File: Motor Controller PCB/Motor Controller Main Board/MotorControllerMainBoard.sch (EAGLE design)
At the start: 83 parts, among them T1 TEENSY_3.1_ALL_PINS

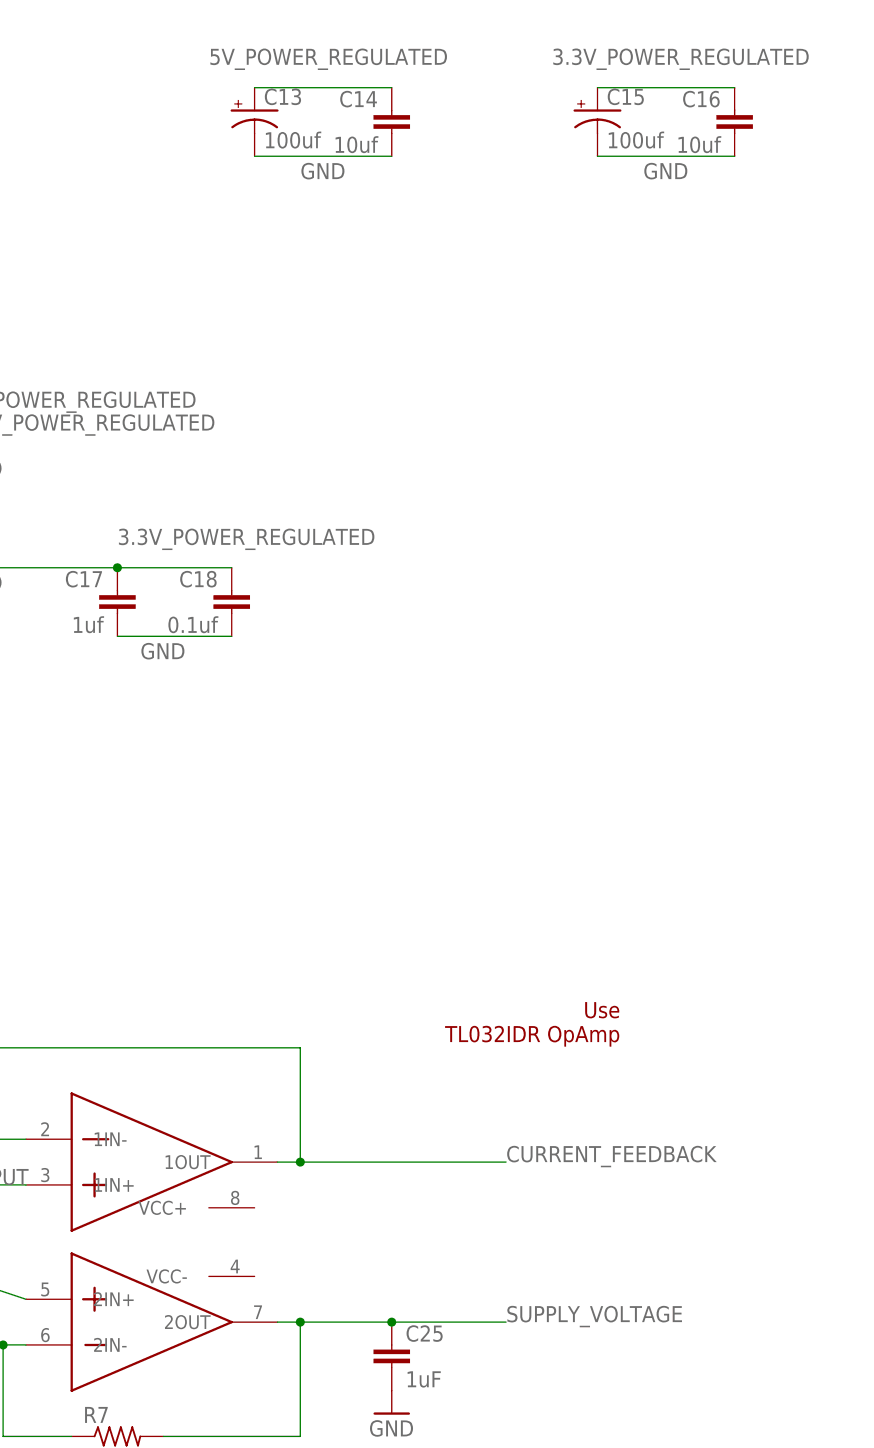
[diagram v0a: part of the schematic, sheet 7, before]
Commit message: Paralleled power capacitors for the teensy
-For both the 5V and 3.3V
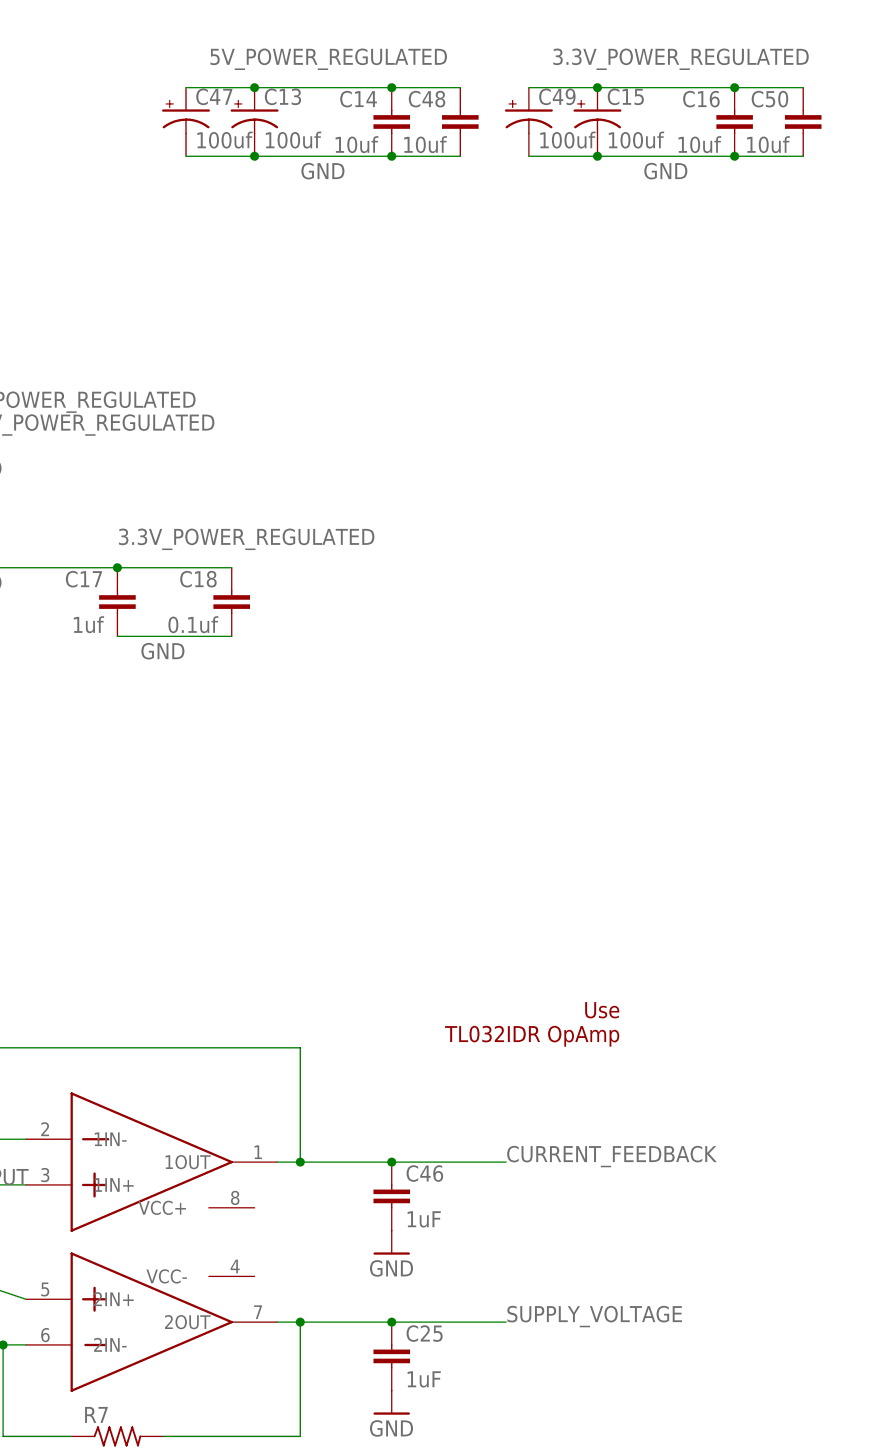
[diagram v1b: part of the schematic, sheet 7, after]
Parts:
- added C46: 1uF, rcl:C-EUC0805
- added C47, C49: 100uf, SparkFun-Capacitors:CAP_POLC
- added C48, C50: 10uf, SparkFun-Capacitors:CAP0805
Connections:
- net 3.3V_POWER_REGULATED: now also C49.+, C50.1
- net 5V_POWER_REGULATED: now also C47.+, C48.1
- net CURRENT_FEEDBACK: now also C46.1
- net GND: now also C46.2, C47.-, C48.2, C49.-, C50.2
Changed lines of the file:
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@@
 <part name="R11" library="MotorControllerEagleLibrary" deviceset="FKN1WSJR-52-4R7" device=""/>
 <part name="R12" library="MotorControllerEagleLibrary" deviceset="FKN1WSJR-52-4R7" device=""/>
+<part name="C46" library="rcl" deviceset="C-EU" device="C0805" value="1uF"/>
+<part name="GND27" library="E-P-008-R1.2" deviceset="GND" device=""/>
+<part name="C47" library="SparkFun-Capacitors" deviceset="CAP_POL" device="C" value="100uf"/>
+<part name="C48" library="SparkFun-Capacitors" deviceset="CAP" device="0805" value="10uf"/>
+<part name="C49" library="SparkFun-Capacitors" deviceset="CAP_POL" device="C" value="100uf"/>
+<part name="C50" library="SparkFun-Capacitors" deviceset="CAP" device="0805" value="10uf"/>
 </parts>
 <sheets>
@@
 <instance part="C23" gate="G$1" x="134.62" y="60.96"/>
 <instance part="GND9" gate="1" x="134.62" y="53.34"/>
+<instance part="C46" gate="G$1" x="213.36" y="76.2"/>
+<instance part="GND27" gate="1" x="213.36" y="68.58"/>
+<instance part="C47" gate="G$1" x="190.5" y="195.58"/>
+<instance part="C48" gate="G$1" x="220.98" y="193.04" rot="MR0"/>
+<instance part="C49" gate="G$1" x="228.6" y="195.58"/>
+<instance part="C50" gate="G$1" x="259.08" y="193.04" rot="MR0"/>
 </instances>
 <busses>
@@
 <label x="203.2" y="187.96" size="1.778" layer="95"/>
 <pinref part="C14" gate="G$1" pin="2"/>
+<pinref part="C47" gate="G$1" pin="-"/>
+<wire x1="190.5" y1="190.5" x2="198.12" y2="190.5" width="0.1524" layer="91"/>
+<junction x="198.12" y="190.5"/>
+<pinref part="C48" gate="G$1" pin="2"/>
+<wire x1="213.36" y1="190.5" x2="220.98" y2="190.5" width="0.1524" layer="91"/>
+<junction x="213.36" y="190.5"/>
 </segment>
 <segment>
@@
 <label x="241.3" y="187.96" size="1.778" layer="95"/>
 <pinref part="C16" gate="G$1" pin="2"/>
+<pinref part="C49" gate="G$1" pin="-"/>
+<wire x1="228.6" y1="190.5" x2="236.22" y2="190.5" width="0.1524" layer="91"/>
+<junction x="236.22" y="190.5"/>
+<pinref part="C50" gate="G$1" pin="2"/>
+<wire x1="251.46" y1="190.5" x2="259.08" y2="190.5" width="0.1524" layer="91"/>
+<junction x="251.46" y="190.5"/>
 </segment>
 <segment>
@@
 <pinref part="GND9" gate="1" pin="GND"/>
 </segment>
+<segment>
+<pinref part="C46" gate="G$1" pin="2"/>
+<pinref part="GND27" gate="1" pin="GND"/>
+</segment>
 </net>
 <net name="5V_POWER_REGULATED" class="0">
@@
 <wire x1="198.12" y1="198.12" x2="213.36" y2="198.12" width="0.1524" layer="91"/>
 <label x="193.04" y="200.66" size="1.778" layer="95"/>
+<pinref part="C47" gate="G$1" pin="+"/>
+<wire x1="190.5" y1="198.12" x2="198.12" y2="198.12" width="0.1524" layer="91"/>
+<junction x="198.12" y="198.12"/>
+<pinref part="C48" gate="G$1" pin="1"/>
+<wire x1="213.36" y1="198.12" x2="220.98" y2="198.12" width="0.1524" layer="91"/>
+<junction x="213.36" y="198.12"/>
 </segment>
 <segment>
@@
 <wire x1="236.22" y1="198.12" x2="251.46" y2="198.12" width="0.1524" layer="91"/>
 <label x="231.14" y="200.66" size="1.778" layer="95"/>
+<pinref part="C49" gate="G$1" pin="+"/>
+<wire x1="228.6" y1="198.12" x2="236.22" y2="198.12" width="0.1524" layer="91"/>
+<junction x="236.22" y="198.12"/>
+<pinref part="C50" gate="G$1" pin="1"/>
+<wire x1="251.46" y1="198.12" x2="259.08" y2="198.12" width="0.1524" layer="91"/>
+<junction x="251.46" y="198.12"/>
 </segment>
 <segment>
@@
 <wire x1="203.2" y1="78.74" x2="200.66" y2="78.74" width="0.1524" layer="91"/>
 <junction x="203.2" y="78.74"/>
-<wire x1="203.2" y1="78.74" x2="226.06" y2="78.74" width="0.1524" layer="91"/>
+<wire x1="203.2" y1="78.74" x2="213.36" y2="78.74" width="0.1524" layer="91"/>
 <label x="226.06" y="78.74" size="1.778" layer="95"/>
-</segment>
-</net>
+<pinref part="C46" gate="G$1" pin="1"/>
+<wire x1="213.36" y1="78.74" x2="226.06" y2="78.74" width="0.1524" layer="91"/>
+<junction x="213.36" y="78.74"/>
+</segment>
+</net>

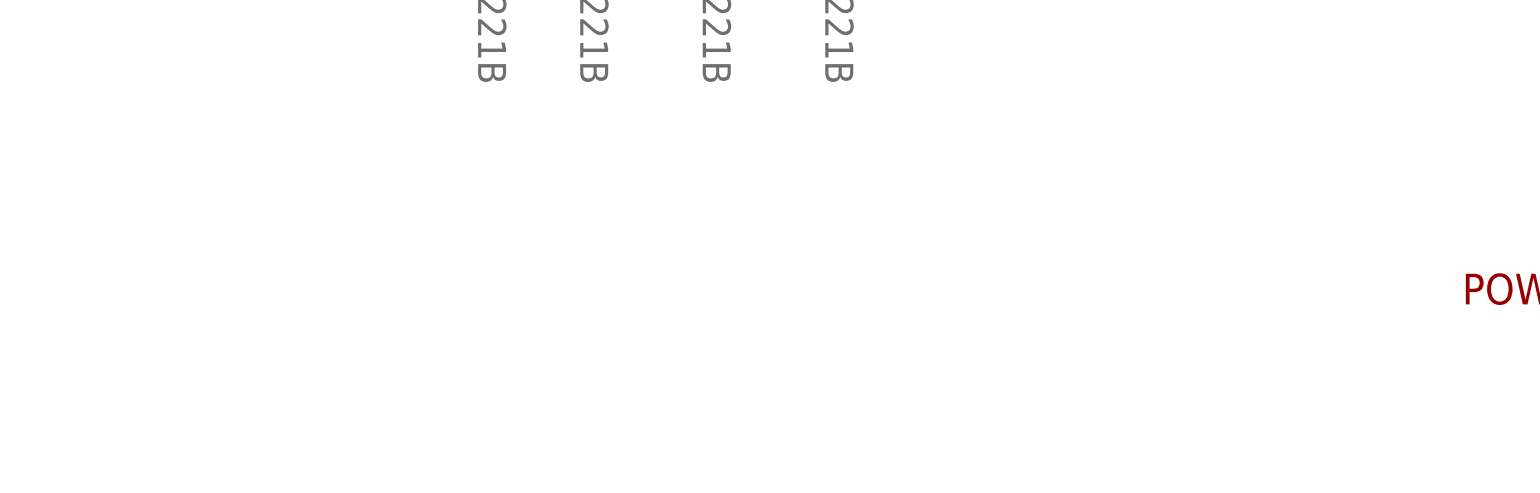
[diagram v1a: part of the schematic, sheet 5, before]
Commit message: Added Negative 12V regulator for op-amps
-Added a -12V regulator for the op-amps. Low power, simple charge pump
that inverts the 12V regulator that already exists on the board.
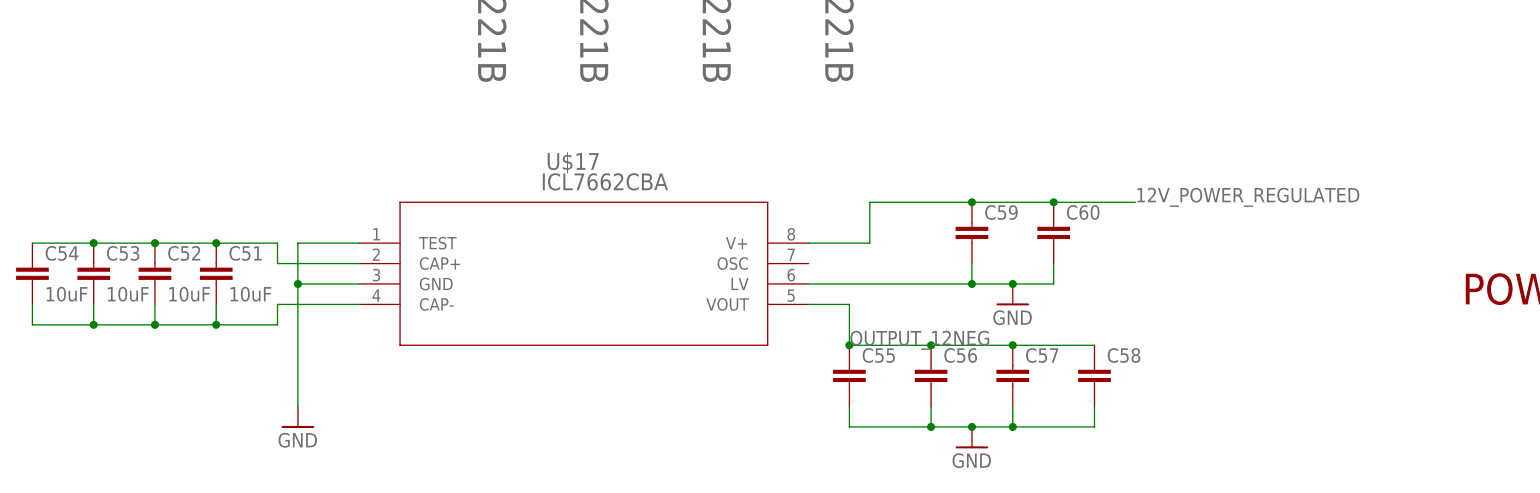
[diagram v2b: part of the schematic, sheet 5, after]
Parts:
- added C51, C52, C53, C54: 10uF, resistor:C-EUC0805
- added C55, C56, C57, C58, C59, C60: (no value), resistor:C-EUC0805
- added U$17: ICL7662CBA, linear:ICL7662CBA
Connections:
- new net N$14: C51.1, C52.1, C53.1, C54.1, U$17.CAP+
- new net N$15: C51.2, C52.2, C53.2, C54.2, U$17.CAP-
- new net OUTPUT_12NEG: AD8512ARZ.VCC-, C55.1, C56.1, C57.1, C58.1, U$17.VOUT
- net 12V_POWER_REGULATED: now also AD8512ARZ.VCC+, C59.1, C60.1, U$17.V+
- net GND: now also C55.2, C56.2, C57.2, C58.2, C59.2, C60.2, U$17.GND, U$17.LV, U$17.TEST
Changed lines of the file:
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@@
 <part name="C49" library="SparkFun-Capacitors" deviceset="CAP_POL" device="C" value="100uf"/>
 <part name="C50" library="SparkFun-Capacitors" deviceset="CAP" device="0805" value="10uf"/>
+<part name="U$17" library="linear" deviceset="ICL7662CBA" device=""/>
+<part name="GND28" library="E-P-008-R1.2" deviceset="GND" device=""/>
+<part name="C51" library="resistor" library_urn="urn:adsk.eagle:library:348" deviceset="C-EU" device="C0805" package3d_urn="urn:adsk.eagle:package:26137/1" value="10uF"/>
+<part name="C52" library="resistor" library_urn="urn:adsk.eagle:library:348" deviceset="C-EU" device="C0805" package3d_urn="urn:adsk.eagle:package:26137/1" value="10uF"/>
+<part name="C53" library="resistor" library_urn="urn:adsk.eagle:library:348" deviceset="C-EU" device="C0805" package3d_urn="urn:adsk.eagle:package:26137/1" value="10uF"/>
+<part name="C54" library="resistor" library_urn="urn:adsk.eagle:library:348" deviceset="C-EU" device="C0805" package3d_urn="urn:adsk.eagle:package:26137/1" value="10uF"/>
+<part name="C55" library="resistor" library_urn="urn:adsk.eagle:library:348" deviceset="C-EU" device="C0805" package3d_urn="urn:adsk.eagle:package:26137/1"/>
+<part name="C56" library="resistor" library_urn="urn:adsk.eagle:library:348" deviceset="C-EU" device="C0805" package3d_urn="urn:adsk.eagle:package:26137/1"/>
+<part name="C57" library="resistor" library_urn="urn:adsk.eagle:library:348" deviceset="C-EU" device="C0805" package3d_urn="urn:adsk.eagle:package:26137/1"/>
+<part name="C58" library="resistor" library_urn="urn:adsk.eagle:library:348" deviceset="C-EU" device="C0805" package3d_urn="urn:adsk.eagle:package:26137/1"/>
+<part name="C59" library="resistor" library_urn="urn:adsk.eagle:library:348" deviceset="C-EU" device="C0805" package3d_urn="urn:adsk.eagle:package:26137/1"/>
+<part name="C60" library="resistor" library_urn="urn:adsk.eagle:library:348" deviceset="C-EU" device="C0805" package3d_urn="urn:adsk.eagle:package:26137/1"/>
+<part name="GND29" library="E-P-008-R1.2" deviceset="GND" device=""/>
+<part name="GND30" library="E-P-008-R1.2" deviceset="GND" device=""/>
 </parts>
 <sheets>
@@
 <instance part="GND22" gate="1" x="66.04" y="99.06"/>
 <instance part="GND23" gate="1" x="66.04" y="172.72"/>
+<instance part="U$17" gate="G$1" x="60.96" y="35.56"/>
+<instance part="GND28" gate="1" x="55.88" y="12.7"/>
+<instance part="C51" gate="G$1" x="45.72" y="33.02"/>
+<instance part="C52" gate="G$1" x="38.1" y="33.02"/>
+<instance part="C53" gate="G$1" x="30.48" y="33.02"/>
+<instance part="C54" gate="G$1" x="22.86" y="33.02"/>
+<instance part="C55" gate="G$1" x="124.46" y="20.32"/>
+<instance part="C56" gate="G$1" x="134.62" y="20.32"/>
+<instance part="C57" gate="G$1" x="144.78" y="20.32"/>
+<instance part="C58" gate="G$1" x="154.94" y="20.32"/>
+<instance part="C59" gate="G$1" x="139.7" y="38.1"/>
+<instance part="C60" gate="G$1" x="149.86" y="38.1"/>
+<instance part="GND29" gate="1" x="144.78" y="27.94"/>
+<instance part="GND30" gate="1" x="139.7" y="10.16"/>
 </instances>
 <busses>
@@
 <pinref part="U$13" gate="A" pin="GND"/>
 <pinref part="GND22" gate="1" pin="GND"/>
+</segment>
+<segment>
+<pinref part="U$17" gate="G$1" pin="TEST"/>
+<wire x1="63.5" y1="35.56" x2="55.88" y2="35.56" width="0.1524" layer="91"/>
+<wire x1="55.88" y1="35.56" x2="55.88" y2="30.48" width="0.1524" layer="91"/>
+<pinref part="U$17" gate="G$1" pin="GND"/>
+<wire x1="55.88" y1="30.48" x2="55.88" y2="15.24" width="0.1524" layer="91"/>
+<wire x1="63.5" y1="30.48" x2="55.88" y2="30.48" width="0.1524" layer="91"/>
+<junction x="55.88" y="30.48"/>
+<pinref part="GND28" gate="1" pin="GND"/>
+</segment>
+<segment>
+<pinref part="U$17" gate="G$1" pin="LV"/>
+<pinref part="C59" gate="G$1" pin="2"/>
+<wire x1="119.38" y1="30.48" x2="139.7" y2="30.48" width="0.1524" layer="91"/>
+<wire x1="139.7" y1="30.48" x2="139.7" y2="33.02" width="0.1524" layer="91"/>
+<pinref part="C60" gate="G$1" pin="2"/>
+<wire x1="139.7" y1="30.48" x2="144.78" y2="30.48" width="0.1524" layer="91"/>
+<wire x1="144.78" y1="30.48" x2="149.86" y2="30.48" width="0.1524" layer="91"/>
+<wire x1="149.86" y1="30.48" x2="149.86" y2="33.02" width="0.1524" layer="91"/>
+<junction x="139.7" y="30.48"/>
+<pinref part="GND29" gate="1" pin="GND"/>
+<junction x="144.78" y="30.48"/>
+</segment>
+<segment>
+<pinref part="C55" gate="G$1" pin="2"/>
+<wire x1="124.46" y1="15.24" x2="124.46" y2="12.7" width="0.1524" layer="91"/>
+<pinref part="C58" gate="G$1" pin="2"/>
+<wire x1="124.46" y1="12.7" x2="134.62" y2="12.7" width="0.1524" layer="91"/>
+<wire x1="134.62" y1="12.7" x2="139.7" y2="12.7" width="0.1524" layer="91"/>
+<wire x1="139.7" y1="12.7" x2="144.78" y2="12.7" width="0.1524" layer="91"/>
+<wire x1="144.78" y1="12.7" x2="154.94" y2="12.7" width="0.1524" layer="91"/>
+<wire x1="154.94" y1="12.7" x2="154.94" y2="15.24" width="0.1524" layer="91"/>
+<pinref part="C57" gate="G$1" pin="2"/>
+<wire x1="144.78" y1="15.24" x2="144.78" y2="12.7" width="0.1524" layer="91"/>
+<junction x="144.78" y="12.7"/>
+<pinref part="C56" gate="G$1" pin="2"/>
+<wire x1="134.62" y1="15.24" x2="134.62" y2="12.7" width="0.1524" layer="91"/>
+<junction x="134.62" y="12.7"/>
+<pinref part="GND30" gate="1" pin="GND"/>
+<junction x="139.7" y="12.7"/>
 </segment>
 </net>
@@
 <wire x1="104.14" y1="175.26" x2="127" y2="175.26" width="0.1524" layer="91"/>
 </segment>
+<segment>
+<pinref part="U$17" gate="G$1" pin="V+"/>
+<wire x1="119.38" y1="35.56" x2="127" y2="35.56" width="0.1524" layer="91"/>
+<wire x1="127" y1="35.56" x2="127" y2="40.64" width="0.1524" layer="91"/>
+<pinref part="C59" gate="G$1" pin="1"/>
+<wire x1="127" y1="40.64" x2="139.7" y2="40.64" width="0.1524" layer="91"/>
+<pinref part="C60" gate="G$1" pin="1"/>
+<wire x1="139.7" y1="40.64" x2="149.86" y2="40.64" width="0.1524" layer="91"/>
+<junction x="139.7" y="40.64"/>
+<wire x1="149.86" y1="40.64" x2="160.02" y2="40.64" width="0.1524" layer="91"/>
+<junction x="149.86" y="40.64"/>
+<label x="160.02" y="40.64" size="1.778" layer="95"/>
+</segment>
 </net>
 <net name="N$1" class="0">
@@
 <wire x1="68.58" y1="106.68" x2="66.04" y2="106.68" width="0.1524" layer="91"/>
 <label x="50.8" y="106.68" size="1.778" layer="95"/>
+</segment>
+</net>
+<net name="N$14" class="0">
+<segment>
+<pinref part="C54" gate="G$1" pin="1"/>
+<pinref part="C53" gate="G$1" pin="1"/>
+<wire x1="22.86" y1="35.56" x2="30.48" y2="35.56" width="0.1524" layer="91"/>
+<pinref part="C52" gate="G$1" pin="1"/>
+<wire x1="30.48" y1="35.56" x2="38.1" y2="35.56" width="0.1524" layer="91"/>
+<junction x="30.48" y="35.56"/>
+<pinref part="C51" gate="G$1" pin="1"/>
+<wire x1="38.1" y1="35.56" x2="45.72" y2="35.56" width="0.1524" layer="91"/>
+<junction x="38.1" y="35.56"/>
+<wire x1="45.72" y1="35.56" x2="53.34" y2="35.56" width="0.1524" layer="91"/>
+<wire x1="53.34" y1="35.56" x2="53.34" y2="33.02" width="0.1524" layer="91"/>
+<junction x="45.72" y="35.56"/>
+<pinref part="U$17" gate="G$1" pin="CAP+"/>
+<wire x1="53.34" y1="33.02" x2="63.5" y2="33.02" width="0.1524" layer="91"/>
+</segment>
+</net>
+<net name="N$15" class="0">
+<segment>
+<pinref part="C54" gate="G$1" pin="2"/>
+<wire x1="22.86" y1="27.94" x2="22.86" y2="25.4" width="0.1524" layer="91"/>
+<pinref part="C51" gate="G$1" pin="2"/>
+<wire x1="22.86" y1="25.4" x2="30.48" y2="25.4" width="0.1524" layer="91"/>
+<wire x1="30.48" y1="25.4" x2="38.1" y2="25.4" width="0.1524" layer="91"/>
+<wire x1="45.72" y1="25.4" x2="45.72" y2="27.94" width="0.1524" layer="91"/>
+<pinref part="C52" gate="G$1" pin="2"/>
+<wire x1="38.1" y1="27.94" x2="38.1" y2="25.4" width="0.1524" layer="91"/>
+<junction x="38.1" y="25.4"/>
+<pinref part="C53" gate="G$1" pin="2"/>
+<wire x1="30.48" y1="27.94" x2="30.48" y2="25.4" width="0.1524" layer="91"/>
+<junction x="30.48" y="25.4"/>
+<wire x1="38.1" y1="25.4" x2="45.72" y2="25.4" width="0.1524" layer="91"/>
+<wire x1="45.72" y1="25.4" x2="53.34" y2="25.4" width="0.1524" layer="91"/>
+<wire x1="53.34" y1="25.4" x2="53.34" y2="27.94" width="0.1524" layer="91"/>
+<junction x="45.72" y="25.4"/>
+<pinref part="U$17" gate="G$1" pin="CAP-"/>
+<wire x1="53.34" y1="27.94" x2="63.5" y2="27.94" width="0.1524" layer="91"/>
+</segment>
+</net>
+<net name="OUTPUT_12NEG" class="0">
+<segment>
+<pinref part="U$17" gate="G$1" pin="VOUT"/>
+<wire x1="119.38" y1="27.94" x2="124.46" y2="27.94" width="0.1524" layer="91"/>
+<pinref part="C55" gate="G$1" pin="1"/>
+<wire x1="124.46" y1="27.94" x2="124.46" y2="22.86" width="0.1524" layer="91"/>
+<pinref part="C56" gate="G$1" pin="1"/>
+<wire x1="124.46" y1="22.86" x2="134.62" y2="22.86" width="0.1524" layer="91"/>
+<junction x="124.46" y="22.86"/>
+<pinref part="C57" gate="G$1" pin="1"/>
+<wire x1="134.62" y1="22.86" x2="144.78" y2="22.86" width="0.1524" layer="91"/>
+<junction x="134.62" y="22.86"/>
+<pinref part="C58" gate="G$1" pin="1"/>
+<wire x1="144.78" y1="22.86" x2="154.94" y2="22.86" width="0.1524" layer="91"/>
+<junction x="144.78" y="22.86"/>
+<label x="124.46" y="22.86" size="1.778" layer="95"/>
 </segment>
 </net>
@@
 </segment>
 </net>
+<net name="12V_POWER_REGULATED" class="0">
+<segment>
+<pinref part="AD8512ARZ" gate="A" pin="VCC+"/>
+<wire x1="198.12" y1="73.66" x2="200.66" y2="73.66" width="0.1524" layer="91"/>
+<label x="182.88" y="71.12" size="1.778" layer="95"/>
+</segment>
+</net>
+<net name="OUTPUT_12NEG" class="0">
+<segment>
+<pinref part="AD8512ARZ" gate="A" pin="VCC-"/>
+<wire x1="198.12" y1="66.04" x2="200.66" y2="66.04" width="0.1524" layer="91"/>
+<label x="190.5" y="63.5" size="1.778" layer="95"/>
+</segment>
+</net>
